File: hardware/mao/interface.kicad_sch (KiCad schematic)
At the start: 27 parts, among them J301 LCD, J302 TOUCH TOP, J303 TOUCH REAR, Q301 AO3400A, SW301 SKQGADE010, U301 DRV5012AEDMRR, U302 DRV5012AEDMRR

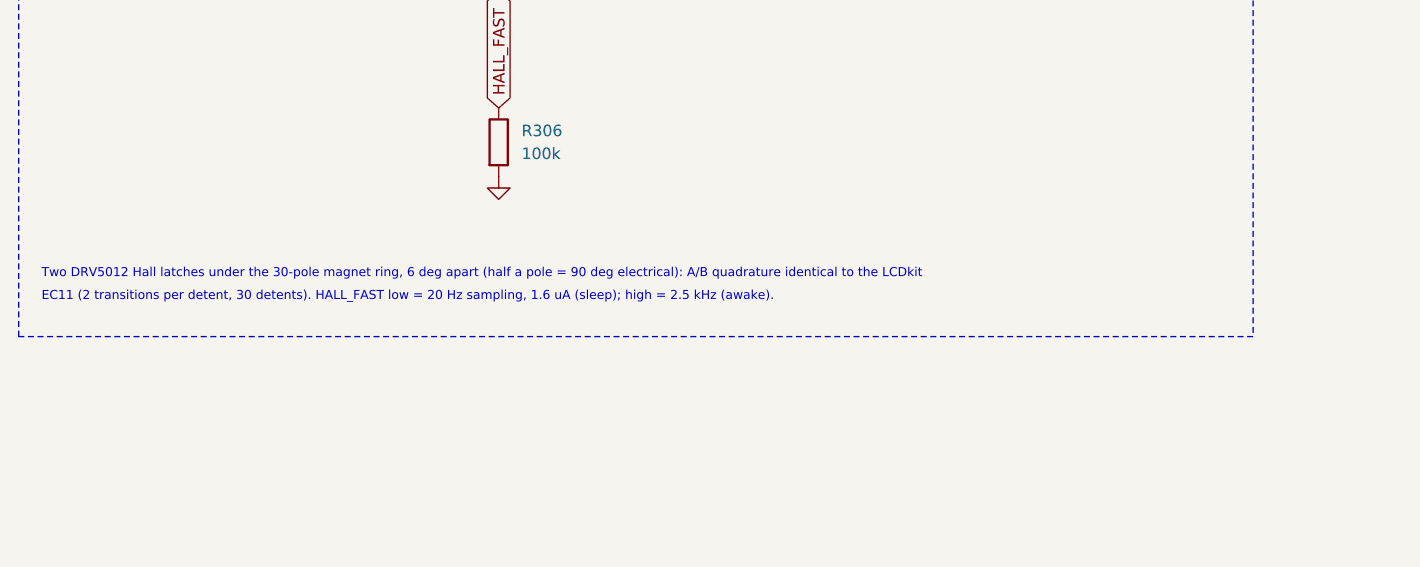
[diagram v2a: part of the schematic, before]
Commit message: MAO A0: speaker that fits, antenna-safe ring, flexure face, haptic input
- Speaker: the specified 15 mm round part did not fit beside the cell. Now a
  Same Sky CMS-150803-088S-X8 (15 x 8 x 3 mm) under the board at 9 o'clock;
  springs J501/J502 replaced by its contact pads LS501 (courtyard keeps B parts
  out). C501/C502 move to F above the amplifier, fed by one via into the L3
  VSYS band; speaker lines are two nested L's on B; LRA pads renamed J501.
- Touch arcs stitched at their ends (2 holes) so none sits under the speaker.
- Ring dial: 30-pole flexible ferrite strip instead of NdFeB discs, so no
  metal sweeps over the antenna; detents are LRA ticks.
- Face: rocks on its lip on three printed flexures (no sliding fit); TOP
  spring boss raised for rim presses.
- Firmware: haptic tick per dial step, click per face press; LEFT touch zone
  holds while the speaker amplifier runs.
- Board rebuilt by the pipeline: DRC/ERC/parity 0, planes one piece,
  194 vias, silk 0 findings, all segments 45 deg; fab, plots, renders and
  Gerber review regenerated. Pipeline rebuilds the footprint cache in place.
- Docs: mechanical spec, review, ODD JOBS compliance, final report,
  bring-up and factory test updated.

Co-Authored-By: Claude Opus 5.5 <noreply@anthropic.com>
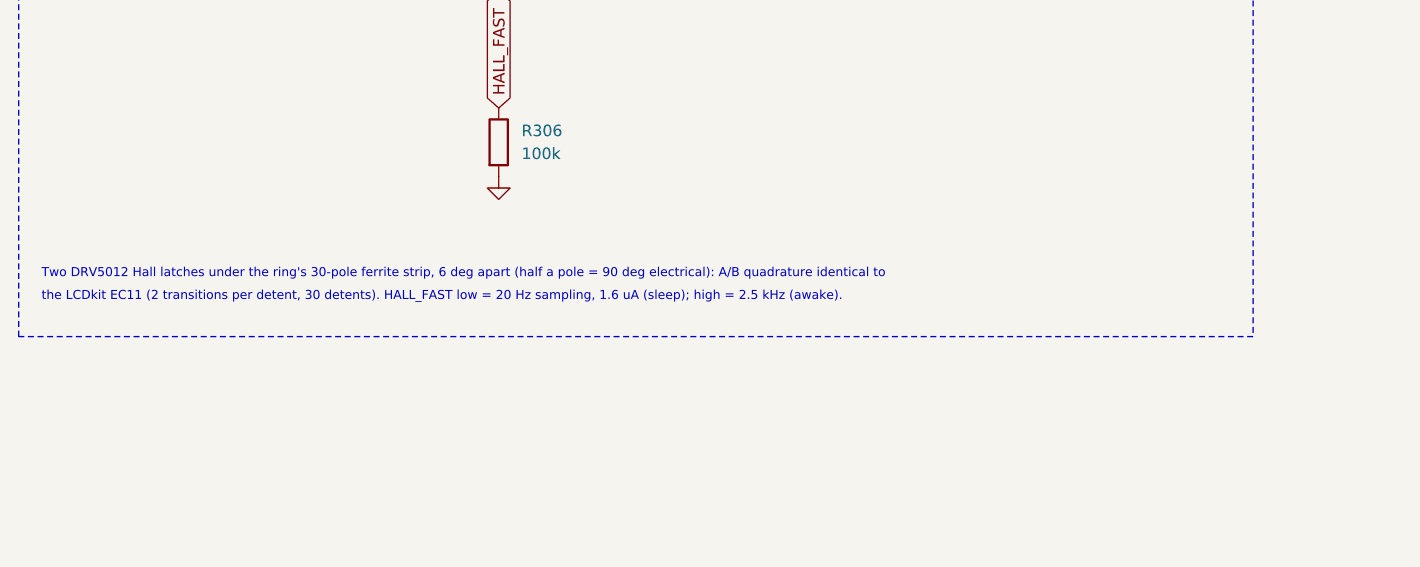
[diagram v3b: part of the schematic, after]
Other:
- note added: "Two DRV5012 Hall latches under the ring's 30-pole ferrite strip, 6 deg apart (half a pole = 90 deg electrical): A/B quadrature identical to"
- note added: "the LCDkit EC11 (2 transitions per detent, 30 detents). HALL_FAST low = 20 Hz sampling, 1.6 uA (sleep); high = 2.5 kHz (awake)."
- note removed: "EC11 (2 transitions per detent, 30 detents). HALL_FAST low = 20 Hz sampling, 1.6 uA (sleep); high = 2.5 kHz (awake)."
- note removed: "Two DRV5012 Hall latches under the 30-pole magnet ring, 6 deg apart (half a pole = 90 deg electrical): A/B quadrature identical to the LCDkit"
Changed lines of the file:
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@@
 		)
 	)
-	(text "Two DRV5012 Hall latches under the 30-pole magnet ring, 6 deg apart (half a pole = 90 deg electrical): A/B quadrature identical to the LCDkit"
+	(text "Two DRV5012 Hall latches under the ring's 30-pole ferrite strip, 6 deg apart (half a pole = 90 deg electrical): A/B quadrature identical to"
 		(exclude_from_sim no)
 		(at 15.24 180.34 0)
@@
 		)
 	)
-	(text "EC11 (2 transitions per detent, 30 detents). HALL_FAST low = 20 Hz sampling, 1.6 uA (sleep); high = 2.5 kHz (awake)."
+	(text "the LCDkit EC11 (2 transitions per detent, 30 detents). HALL_FAST low = 20 Hz sampling, 1.6 uA (sleep); high = 2.5 kHz (awake)."
 		(exclude_from_sim no)
 		(at 15.24 182.88 0)

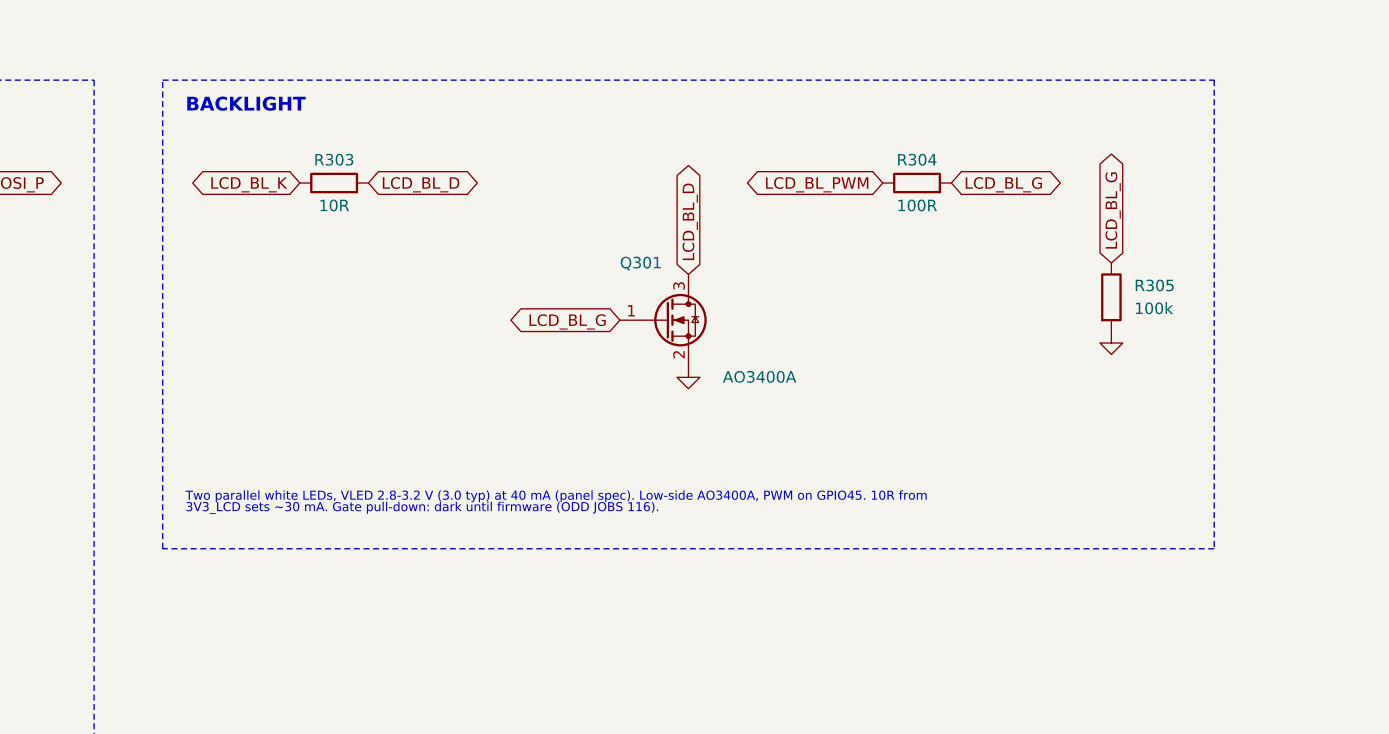
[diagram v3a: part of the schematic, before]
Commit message: MAO A0: circuit simulation suite and the value fixes it found
- hardware/mao/sim: ngspice (KiCad libngspice) + Python suite S1-S15 with
  plots in docs/hardware/sim and results in mao-a0-verification.md
- UVLO divider 470k/240k (was 1M/510k): EN leakage put the worst-case
  cut-off at 2.65 V; now 2.75-3.16 V
- IR LED resistors 56R (was 47R): peaks were 66-70 mA on USB against the
  65 mA rating; now <= 59 mA
- Firmware: 100 % brightness = 80 % backlight PWM, so the 2.8 V panel bin
  averages <= 40 mA
- Docs: speaker power 0.54 W (was quoted as 0.4 W), UVLO, IR, budget,
  bring-up checks for the backlight bin and the ring strip field
- Capture reports fitted and DNP parts separately

Co-Authored-By: Claude Opus 5.5 <noreply@anthropic.com>
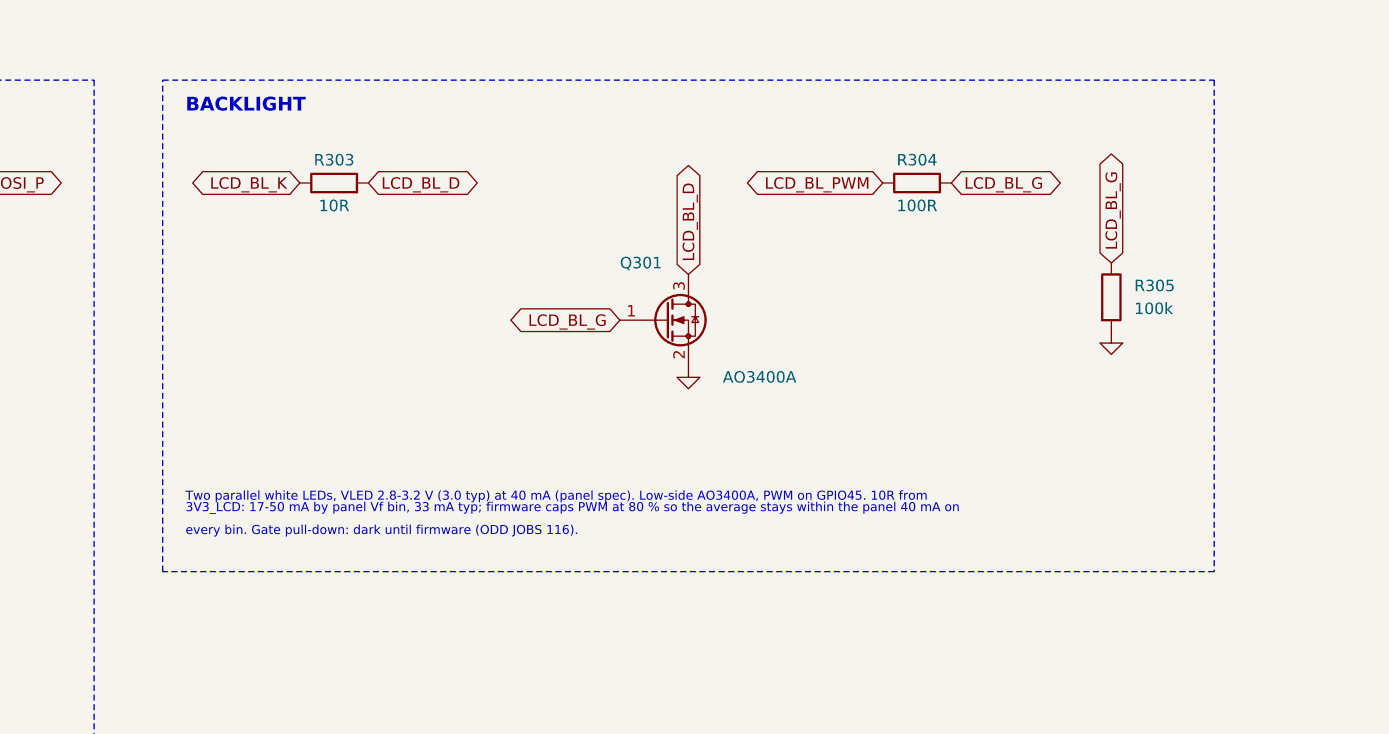
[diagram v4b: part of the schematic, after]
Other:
- note added: "3V3_LCD: 17-50 mA by panel Vf bin, 33 mA typ; firmware caps PWM at 80 % so the average stays within the panel 40 mA on"
- note added: "every bin. Gate pull-down: dark until firmware (ODD JOBS 116)."
- note removed: "3V3_LCD sets ~30 mA. Gate pull-down: dark until firmware (ODD JOBS 116)."
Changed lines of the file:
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@@
 	(rectangle
 		(start 148.59 20.32)
-		(end 265.43 72.39)
+		(end 265.43 74.93)
 		(stroke (width 0.15) (type dash) (color 120 120 120 1))
 		(fill (type none))
@@
 		)
 	)
-	(text "3V3_LCD sets ~30 mA. Gate pull-down: dark until firmware (ODD JOBS 116)."
+	(text "3V3_LCD: 17-50 mA by panel Vf bin, 33 mA typ; firmware caps PWM at 80 % so the average stays within the panel 40 mA on"
 		(exclude_from_sim no)
 		(at 151.13 68.58 0)
 		(effects
 			(font (size 1 1))
+			(justify left bottom)
+		)
+	)
+	(text "every bin. Gate pull-down: dark until firmware (ODD JOBS 116)."
+		(exclude_from_sim no)
+		(at 151.13 71.12 0)
+		(effects
+			(font (size 1 1))
